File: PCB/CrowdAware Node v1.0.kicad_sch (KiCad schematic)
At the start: 6 parts, among them J1 Heltec WiFi LoRa 32(V3)

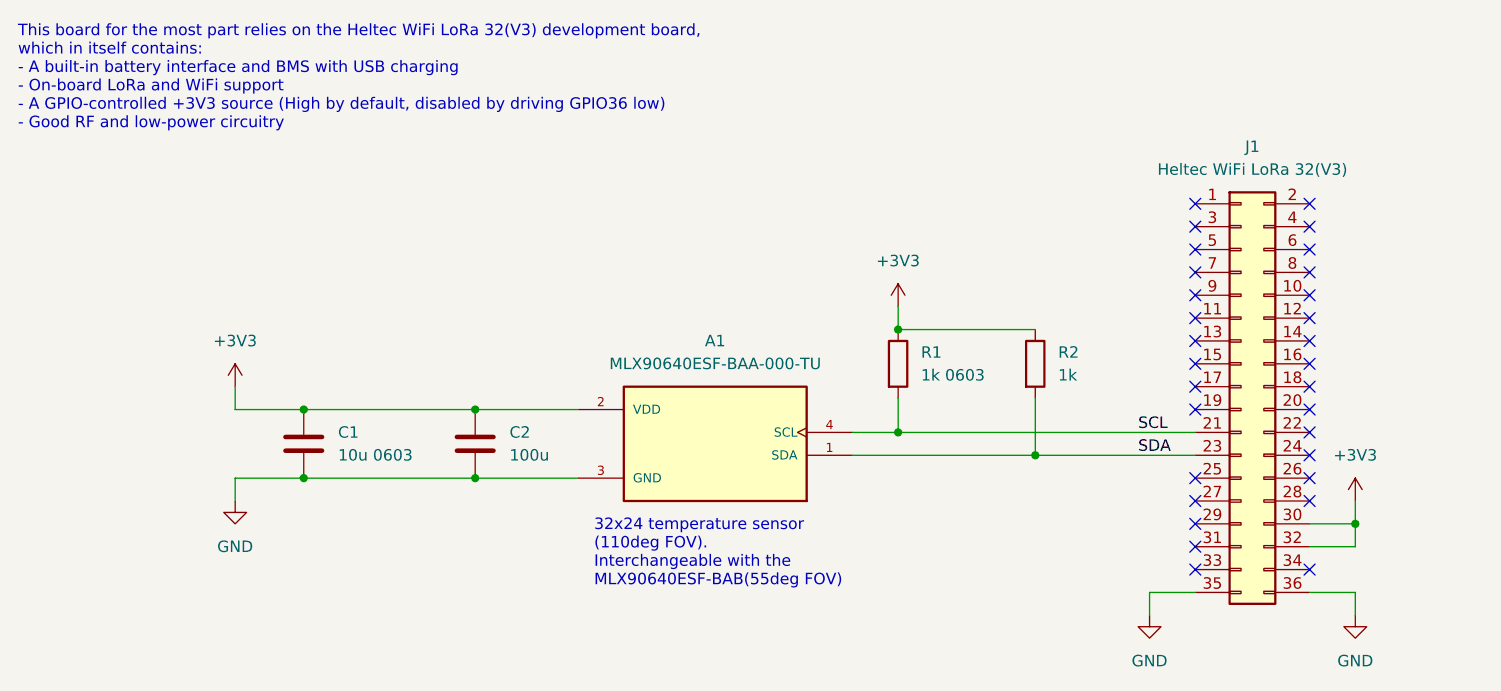
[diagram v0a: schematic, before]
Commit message: Revised routing, changed pullup to 3v3
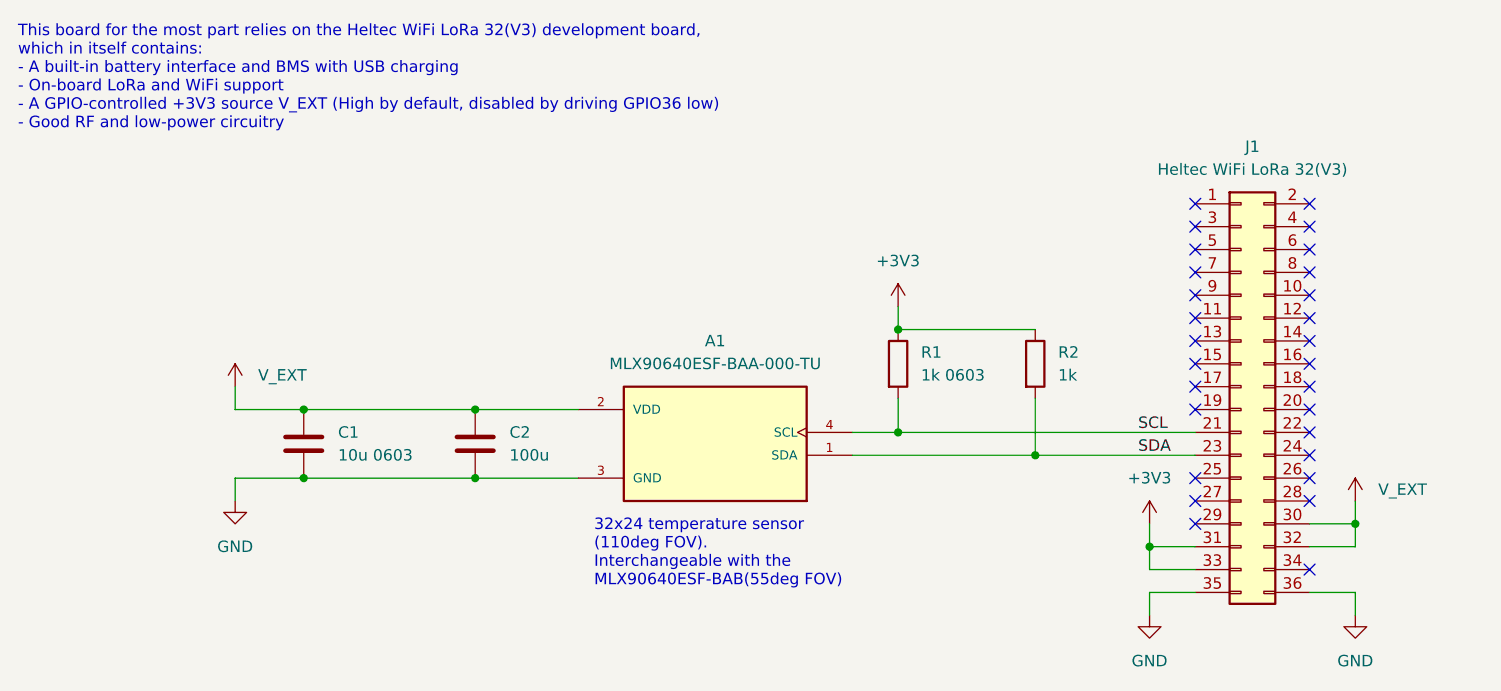
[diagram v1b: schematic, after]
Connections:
- net +3V3: now also J1.31 (Pin_31), J1.33 (Pin_33); no longer A1.2 (VDD), C1.1, C2.1, J1.30 (Pin_30), J1.32 (Pin_32)
- new net V_EXT: A1.2 (VDD), C1.1, C2.1, J1.30 (Pin_30), J1.32 (Pin_32)
- no-connect marks 30 -> 28
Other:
- note added: "This board for the most part relies on the Heltec WiFi LoRa 32(V3) development board, which in itself contains: - A built-in battery interface and BMS with USB charging - On-board LoRa and WiFi support - A GPIO-controlled +3V3 source V_EXT (High by default, disabled by driving GPIO36 low) - Good RF and low-power circuitry"
- note removed: "This board for the most part relies on the Heltec WiFi LoRa 32(V3) development board, which in itself contains: - A built-in battery interface and BMS with USB charging - On-board LoRa and WiFi support - A GPIO-controlled +3V3 source (High by default, disabled by driving GPIO36 low) - Good RF and low-power circuitry"

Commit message: Include BOM, Adjusted footprints to match
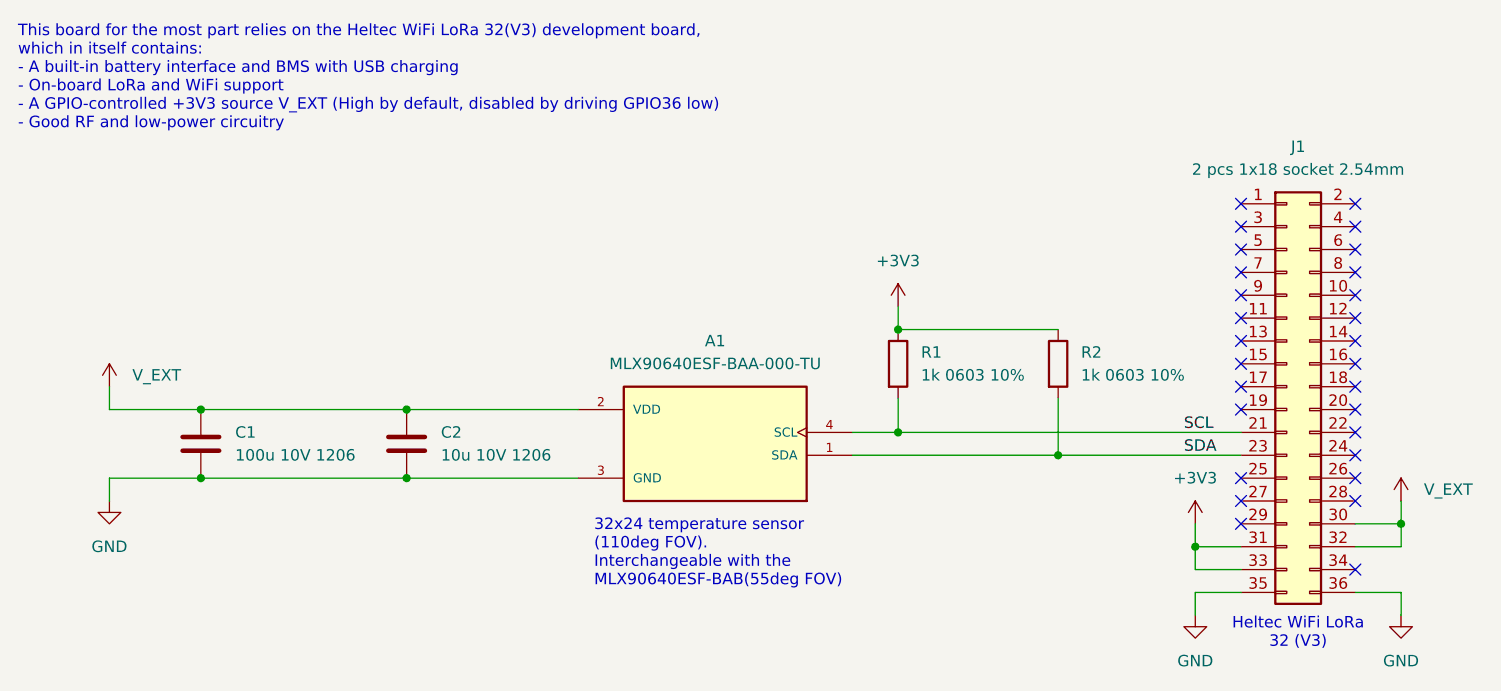
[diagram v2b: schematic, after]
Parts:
- A1: Mouser No. (none) -> 482-MLX90640ESFBAASP
- C1: renamed from C2; value 100u -> 100u 10V 1206; footprint MyLib:C_0603_1608Metric_Pad1.08x0.95mm_HandSolder -> Capacitor_SMD:C_1206_3216Metric_Pad1.33x1.80mm_HandSolder; Mouser No. (none) -> 81-GRM31CR61A107MA8L
- C2: renamed from C1; value 10u 0603 -> 10u 10V 1206; footprint MyLib:C_0603_1608Metric_Pad1.08x0.95mm_HandSolder -> Capacitor_SMD:C_1206_3216Metric_Pad1.33x1.80mm_HandSolder; Mouser No. (none) -> 81-GRM319R61A106KE9J
- J1: value Heltec WiFi LoRa 32(V3) -> 2 pcs 1x18 socket 2.54mm; Mouser No. (none) -> 571-6-535541-6
- R1: value 1k 0603 -> 1k 0603 10%; Mouser No. (none) -> 603-SR0603JR-7T1KL
- R2: value 1k -> 1k 0603 10%; Mouser No. (none) -> 603-SR0603JR-7T1KL
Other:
- note added: "Heltec WiFi LoRa 32 (V3)"
- moved on the sheet: C1, C2, J1, R2
